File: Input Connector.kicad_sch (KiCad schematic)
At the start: 3 parts, among them J1 776228-2, J2 RS-485/CAN, J3 V IN

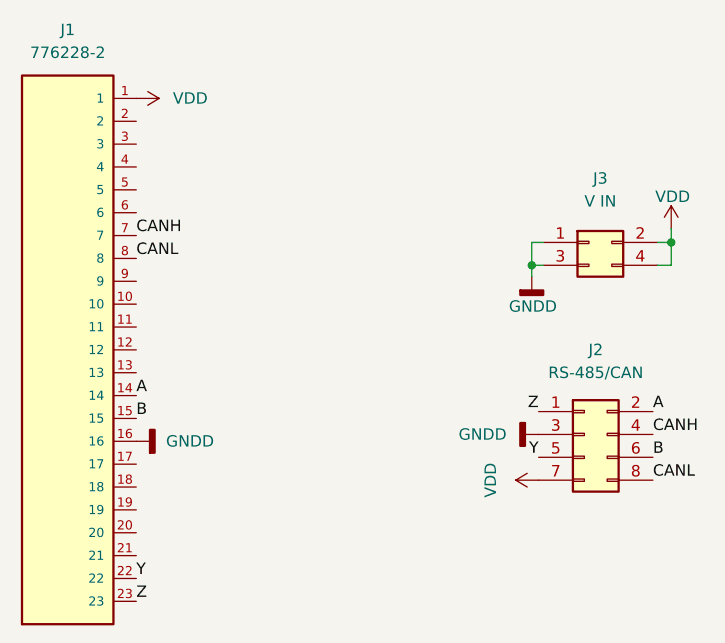
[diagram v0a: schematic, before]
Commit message: Добавил землю RS-484
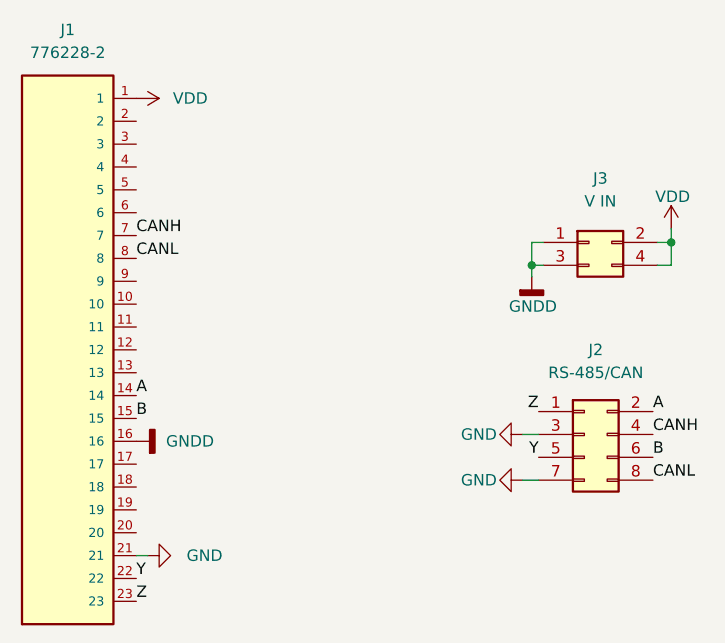
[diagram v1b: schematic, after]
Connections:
- net GNDD: no longer J2.3 (Pin_3)
- net VDD: no longer J2.7 (Pin_7)
- net GND: now reaches J1.21
- net GND: now also J2.3 (Pin_3), J2.7 (Pin_7)
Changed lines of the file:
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@@
   (junction (at 220.218 74.422) (diameter 0) (color 0 0 0 0)
   )
+  (wire (pts (xy 203.708 95.758) (xy 205.486 95.758))
+    (stroke (width 0) (type default) (color 0 0 0 0))
+  )
   (wire (pts (xy 205.994 76.962) (xy 204.724 76.962))
     (stroke (width 0) (type default) (color 0 0 0 0))
@@
     (stroke (width 0) (type default) (color 0 0 0 0))
   )
+  (wire (pts (xy 203.708 100.838) (xy 205.486 100.838))
+    (stroke (width 0) (type default) (color 0 0 0 0))
+  )
   (wire (pts (xy 204.724 76.962) (xy 204.724 78.232))
     (stroke (width 0) (type default) (color 0 0 0 0))
   )
   (wire (pts (xy 205.994 74.422) (xy 204.724 74.422))
+    (stroke (width 0) (type default) (color 0 0 0 0))
+  )
+  (wire (pts (xy 160.782 109.22) (xy 162.052 109.22))
     (stroke (width 0) (type default) (color 0 0 0 0))
   )
@@
   (label "CANH" (at 160.782 73.66 0)
     (effects (font (size 1.27 1.27)) (justify left bottom))
-  )
-  (symbol (lib_id "power:VDD") (at 205.486 100.838 90) (unit 1)
-    (in_bom yes) (on_board yes) (fields_autoplaced)
-    (property "Reference" "#PWR05" (id 0) (at 209.296 100.838 0)
-      (effects (font (size 1.27 1.27)) hide)
-    )
-    (property "Value" "VDD" (id 1) (at 200.152 100.838 0))
-    (property "Footprint" "" (id 2) (at 205.486 100.838 0)
-      (effects (font (size 1.27 1.27)) hide)
-    )
-    (property "Datasheet" "" (id 3) (at 205.486 100.838 0)
-      (effects (font (size 1.27 1.27)) hide)
-    )
-    (pin "1")
   )
   (symbol (lib_id "Connector_Auto:776228-2") (at 153.162 83.82 0) (unit 1)
@@
     (pin "4")
   )
+  (symbol (lib_id "power:GND") (at 203.708 100.838 270) (unit 1)
+    (in_bom yes) (on_board yes)
+    (property "Reference" "#PWR?" (id 0) (at 197.358 100.838 0)
+      (effects (font (size 1.27 1.27)) hide)
+    )
+    (property "Value" "GND" (id 1) (at 196.85 100.838 90)
+      (effects (font (size 1.27 1.27)) (justify left))
+    )
+    (property "Footprint" "" (id 2) (at 203.708 100.838 0)
+      (effects (font (size 1.27 1.27)) hide)
+    )
+    (property "Datasheet" "" (id 3) (at 203.708 100.838 0)
+      (effects (font (size 1.27 1.27)) hide)
+    )
+    (pin "1")
+  )
   (symbol (lib_id "power:GNDD") (at 160.782 96.52 90) (unit 1)
     (in_bom yes) (on_board yes) (fields_autoplaced)
@@
     (pin "1")
   )
+  (symbol (lib_id "power:GND") (at 203.708 95.758 270) (unit 1)
+    (in_bom yes) (on_board yes)
+    (property "Reference" "#PWR?" (id 0) (at 197.358 95.758 0)
+      (effects (font (size 1.27 1.27)) hide)
+    )
+    (property "Value" "GND" (id 1) (at 196.85 95.758 90)
+      (effects (font (size 1.27 1.27)) (justify left))
+    )
+    (property "Footprint" "" (id 2) (at 203.708 95.758 0)
+      (effects (font (size 1.27 1.27)) hide)
+    )
+    (property "Datasheet" "" (id 3) (at 203.708 95.758 0)
+      (effects (font (size 1.27 1.27)) hide)
+    )
+    (pin "1")
+  )
   (symbol (lib_id "power:GNDD") (at 204.724 78.232 0) (unit 1)
     (in_bom yes) (on_board yes)
@@
     )
     (property "Datasheet" "" (id 3) (at 204.724 78.232 0)
+      (effects (font (size 1.27 1.27)) hide)
+    )
+    (pin "1")
+  )
+  (symbol (lib_id "power:GND") (at 162.052 109.22 90) (unit 1)
+    (in_bom yes) (on_board yes) (fields_autoplaced)
+    (property "Reference" "#PWR?" (id 0) (at 168.402 109.22 0)
+      (effects (font (size 1.27 1.27)) hide)
+    )
+    (property "Value" "GND" (id 1) (at 166.37 109.2199 90)
+      (effects (font (size 1.27 1.27)) (justify right))
+    )
+    (property "Footprint" "" (id 2) (at 162.052 109.22 0)
+      (effects (font (size 1.27 1.27)) hide)
+    )
+    (property "Datasheet" "" (id 3) (at 162.052 109.22 0)
       (effects (font (size 1.27 1.27)) hide)
     )
@@
     (pin "1")
   )
-  (symbol (lib_id "power:GNDD") (at 205.486 95.758 270) (unit 1)
-    (in_bom yes) (on_board yes) (fields_autoplaced)
-    (property "Reference" "#PWR04" (id 0) (at 199.136 95.758 0)
-      (effects (font (size 1.27 1.27)) hide)
-    )
-    (property "Value" "GNDD" (id 1) (at 201.93 95.7579 90)
-      (effects (font (size 1.27 1.27)) (justify right))
-    )
-    (property "Footprint" "" (id 2) (at 205.486 95.758 0)
-      (effects (font (size 1.27 1.27)) hide)
-    )
-    (property "Datasheet" "" (id 3) (at 205.486 95.758 0)
-      (effects (font (size 1.27 1.27)) hide)
-    )
-    (pin "1")
-  )
   (symbol (lib_id "power:VDD") (at 160.782 58.42 270) (unit 1)
     (in_bom yes) (on_board yes) (fields_autoplaced)
@@
       (reference "#PWR03") (unit 1) (value "GNDD") (footprint "")
     )
-    (path "/fc74193b-c855-4d23-970a-e3604b574adc"
-      (reference "#PWR04") (unit 1) (value "GNDD") (footprint "")
-    )
-    (path "/22e8f1e9-1595-4a36-8bae-4d31565ffe81"
-      (reference "#PWR05") (unit 1) (value "VDD") (footprint "")
-    )
     (path "/f66ea087-3aef-4bf2-97e0-744dcc5e2151"
       (reference "#PWR06") (unit 1) (value "VDD") (footprint "")
     )
+    (path "/8a96750c-b29a-4aa5-8ff3-afea3afb7e92"
+      (reference "#PWR?") (unit 1) (value "GND") (footprint "")
+    )
+    (path "/a68099d4-407b-45a4-8b28-3b319691f93c"
+      (reference "#PWR?") (unit 1) (value "GND") (footprint "")
+    )
+    (path "/d3c01bbc-067f-4d46-9b64-84ca3aab902a"
+      (reference "#PWR?") (unit 1) (value "GND") (footprint "")
+    )
     (path "/6539cbd1-50bb-4d3c-82f9-984d64bc120e"
